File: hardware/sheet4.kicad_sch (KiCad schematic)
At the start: 16 parts, among them J2 B4B-XH-A, J3 B-2100S04P-A110, U2 STM32F072CBT6

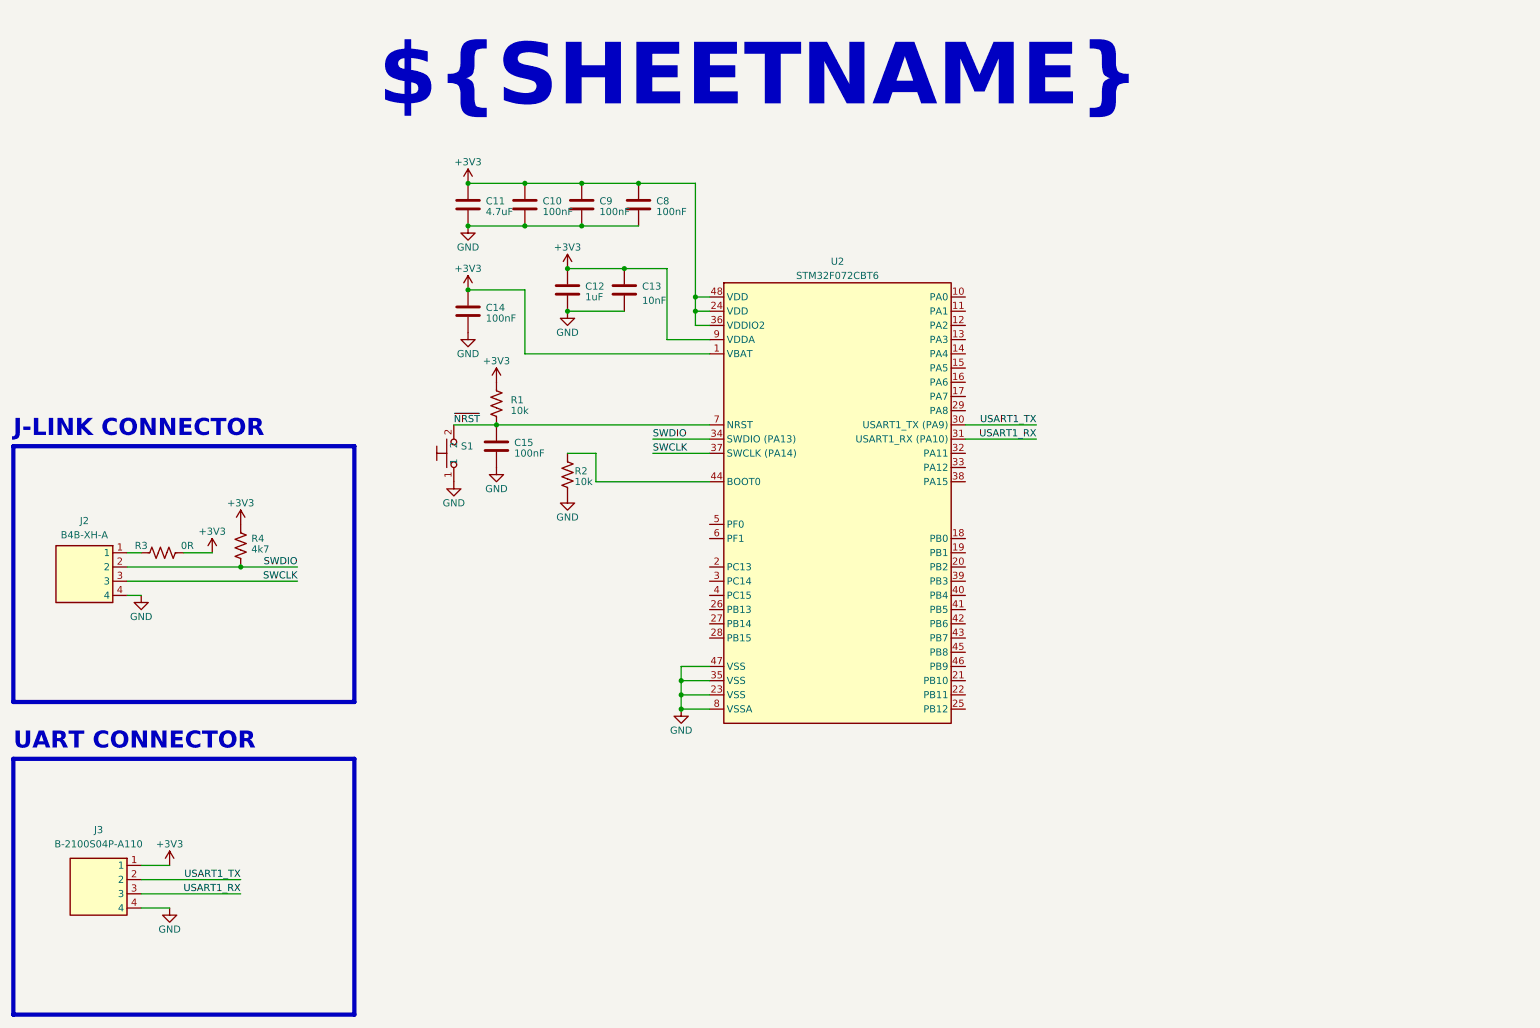
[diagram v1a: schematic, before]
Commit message: hardware(feat): add led indications
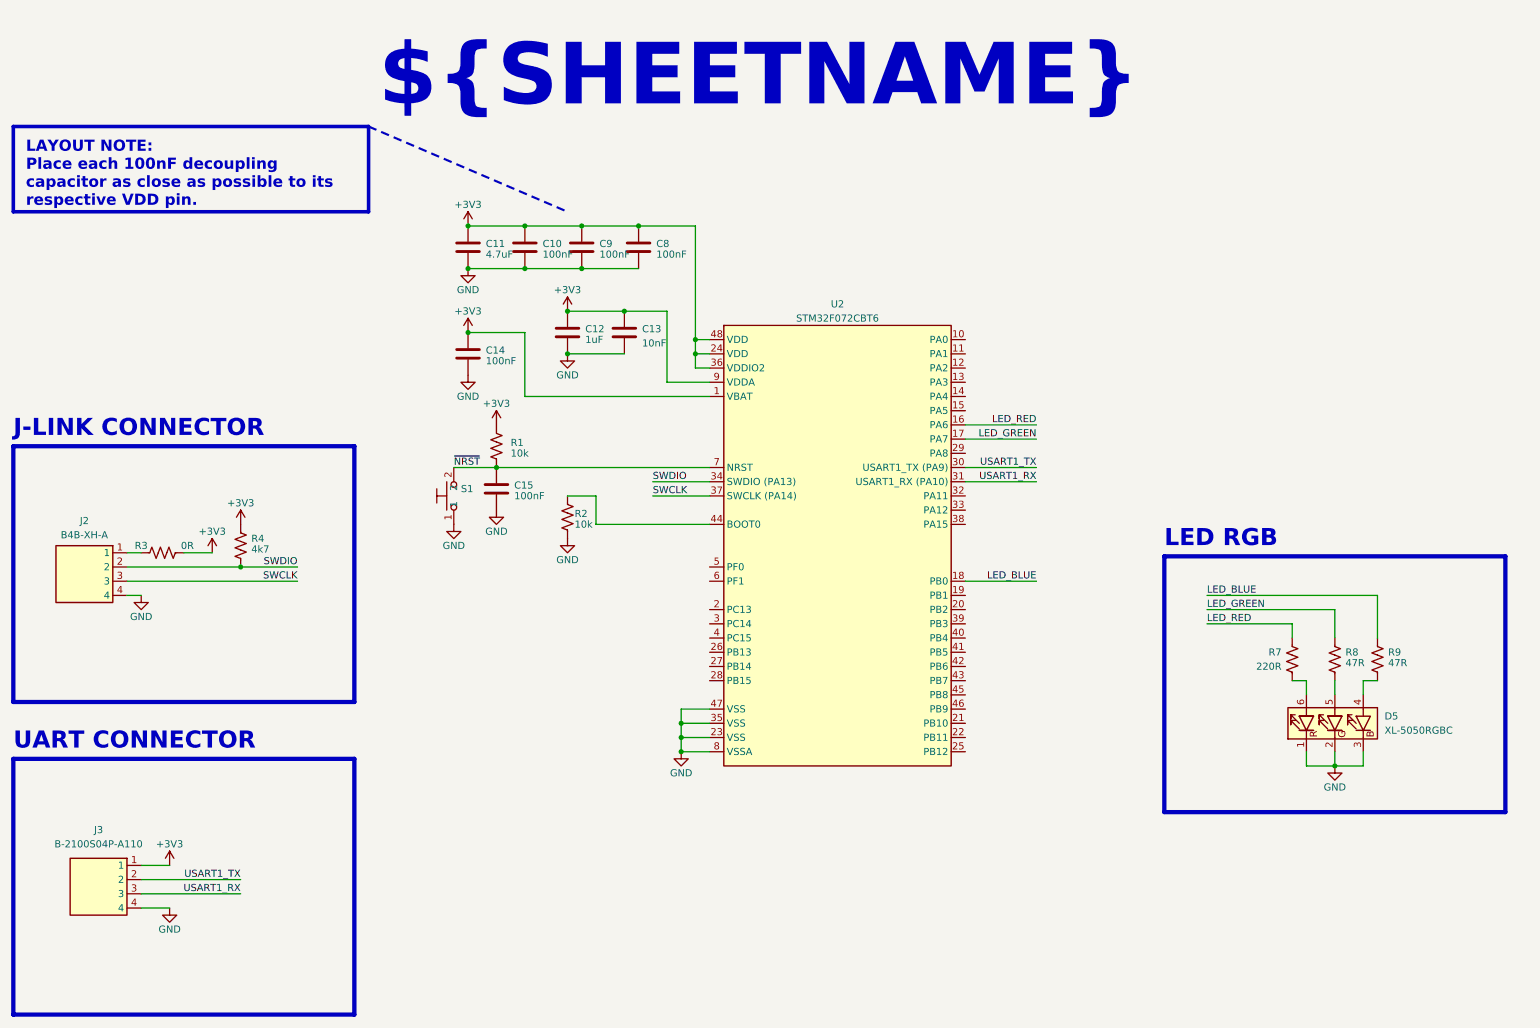
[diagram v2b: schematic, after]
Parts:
- added D5: XL-5050RGBC, 04_diodes:PLCC-6_XL-5050RGBC, symbol 04_diodes:LED_RGB-3.4V-20mA-PLCC-6
- added R7: 220R, 01_resistors:R_0603_1608Metric, symbol 01_resistors:RES_220R-0.1W-1%-0603
- added R8, R9: 47R, 01_resistors:R_0603_1608Metric, symbol 01_resistors:RES_47R-0.1W-1%-0603
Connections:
- net GND: now also D5.1 (RK), D5.2 (GK), D5.3 (BK)
- net LED_RED: now reaches U2.16 (PA6)
- net LED_RED: now also R7.1
- net LED_GREEN: now reaches U2.17 (PA7)
- net LED_GREEN: now also R8.1
- net LED_BLUE: now reaches U2.18 (PB0)
- net LED_BLUE: now also R9.1
- new net: D5.5 (GA), R8.2
- new net: D5.4 (BA), R9.2
- new net: D5.6 (RA), R7.2
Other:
- note added: "LED RGB"
- moved on the sheet: C10, C11, C12, C13, C14, C15, C8, C9, R1, R2, S1, U2

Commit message: hardware(feat): add usb connector with esd (#1)
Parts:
- added C20: 100nF, 02_capacitors:C_0603_1608Metric, symbol 02_capacitors:CAP_100nF-50V-10%-X7R-0603
- added D6: B5819W-TP, 04_diodes:D_SOD-123, symbol 04_diodes:DIO-S_40V-1A-0.6V-SOD-123
- added J4: U254-051N-4BH806, 08_connectors:SMD_U254-051N-4BH806, symbol 08_connectors:CON-USB_U254-051N-4BH806
- added U4: USBLC6-2SC6, 06_ics:SOT-23-6, symbol 06_ics:IC-IF_USBLC6-2SC6
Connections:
- net GND: now also C20.2, J4.5 (GND), J4.6 (SHIELD), U4.2 (GND)
- net USB_D_N: now reaches U2.32 (PA11)
- net USB_D_N: now also U4.3 (I/O2)
- net USB_D_P: now reaches U2.33 (PA12)
- net USB_D_P: now also U4.1 (I/O1)
- new net: J4.2 (D-), U4.4 (I/O2)
- new net: J4.3 (D+), U4.6 (I/O1)
- new net +5V: D6.1 (K)
- new net +VBUS: C20.1, D6.2 (A), J4.1 (VBUS), U4.5 (VBUS)
- no-connect marks 0 -> 1
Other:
- note added: "USB"

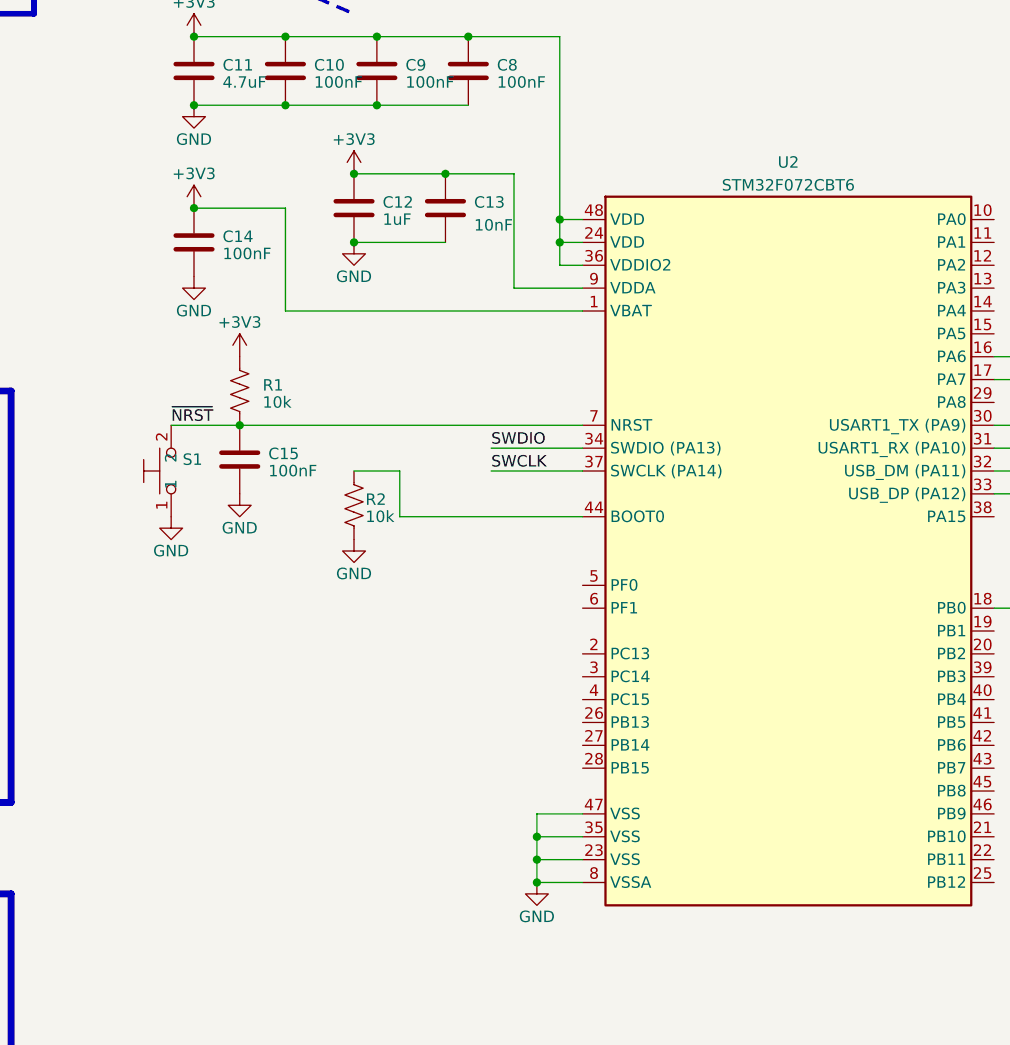
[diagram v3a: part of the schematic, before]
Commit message: hardware(feat): add rtc battery and lse crystal (#2)
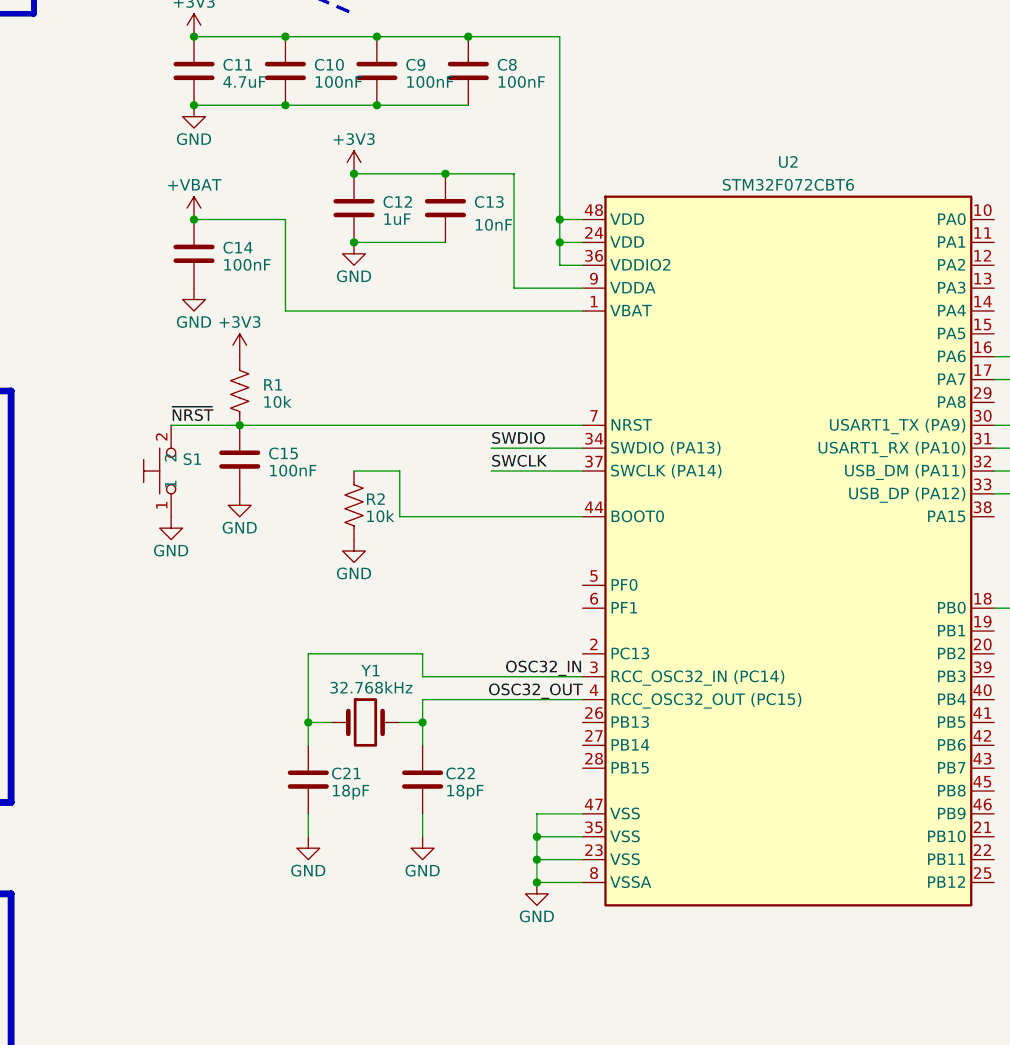
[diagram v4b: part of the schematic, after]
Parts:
- added C21, C22: 18pF, 02_capacitors:C_0603_1608Metric, symbol 02_capacitors:CAP_18pF-50V-5%-C0G-0603
- added Y1: 32.768kHz, 07_crystals:Crystal_SMD_3215-2Pin_3.2x1.5mm, symbol 07_crystals:XTAL_32.768kHz-Q13FC1350000400
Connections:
- net +3V3: no longer C14.1, U2.1 (VBAT)
- net GND: now also C21.2, C22.2
- net OSC32_IN: now reaches U2.3 (PC14)
- net OSC32_IN: now also C21.1, Y1.1
- net OSC32_OUT: now reaches U2.4 (PC15)
- net OSC32_OUT: now also C22.1, Y1.2
- new net +VBAT: C14.1, U2.1 (VBAT)
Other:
- moved on the sheet: C14

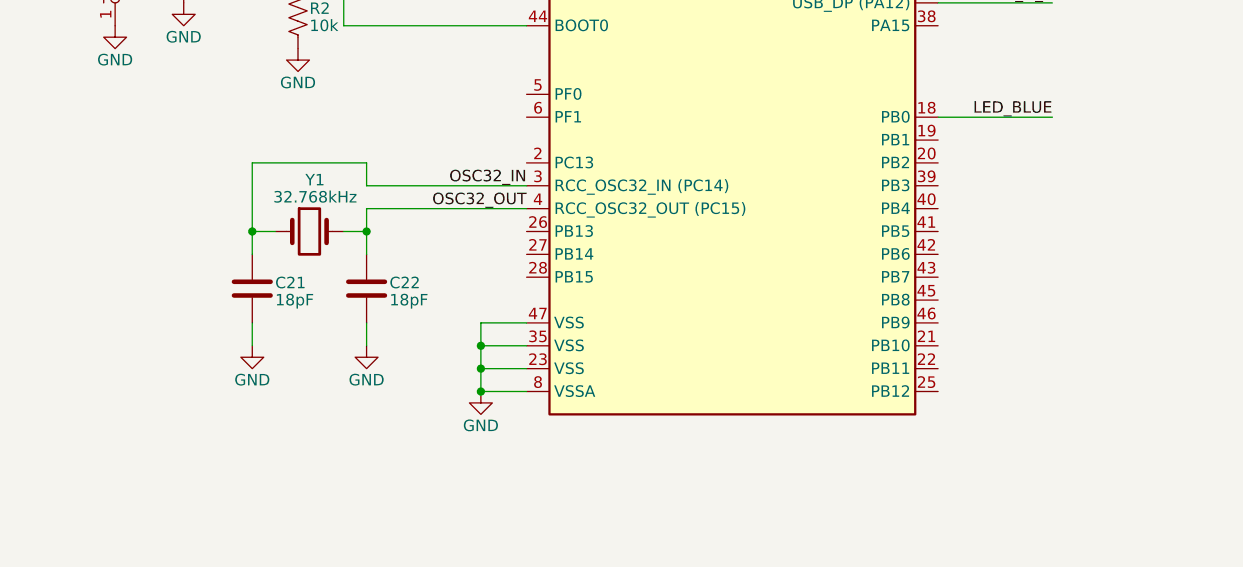
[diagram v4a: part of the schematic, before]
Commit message: hardware(feat): add spi nor flash with cs pull-up and decoupling (#6)
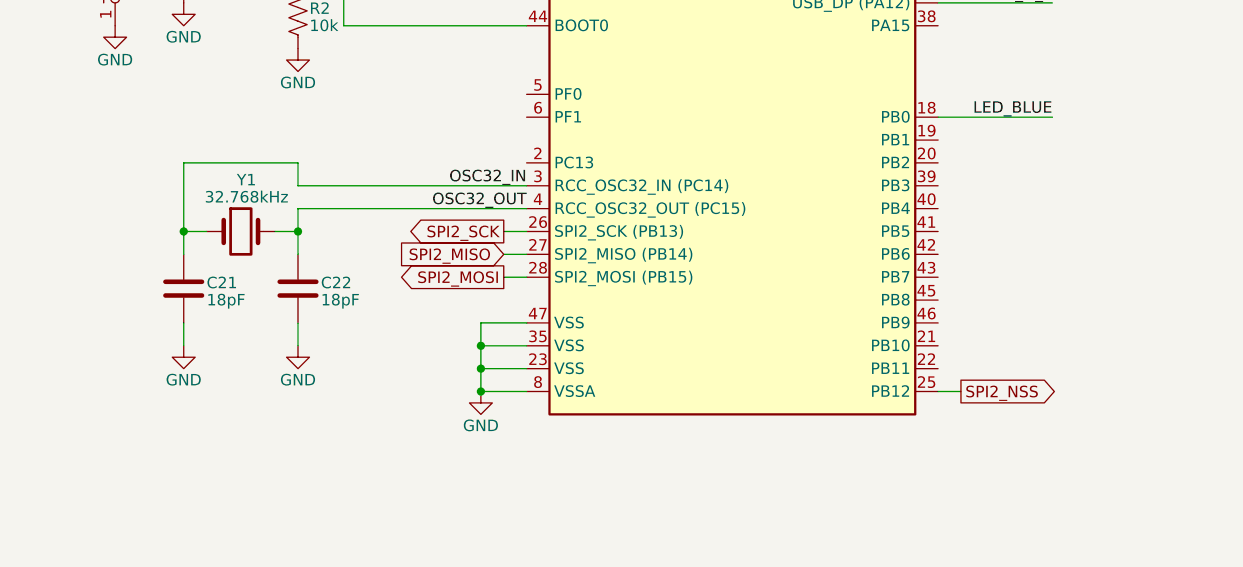
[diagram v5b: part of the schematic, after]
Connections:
- net SPI2_NSS: now reaches U2.25 (PB12)
- net SPI2_SCK: now reaches U2.26 (PB13)
- net SPI2_MISO: now reaches U2.27 (PB14)
- net SPI2_MOSI: now reaches U2.28 (PB15)
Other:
- moved on the sheet: C21, C22, Y1

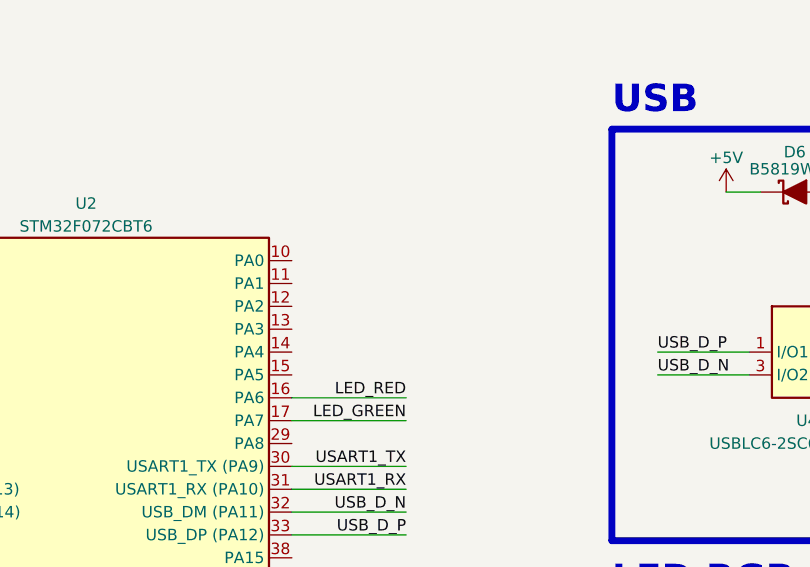
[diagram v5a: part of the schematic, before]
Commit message: hardware(feat): add push buttons with pull-ups and debounce (#3)
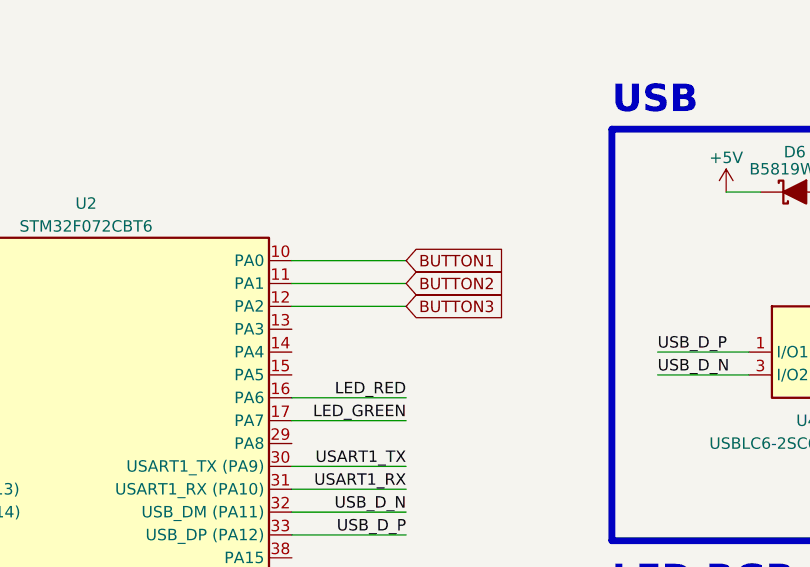
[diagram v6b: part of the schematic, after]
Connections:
- net BUTTON1: now reaches U2.10 (PA0)
- net BUTTON2: now reaches U2.11 (PA1)
- net BUTTON3: now reaches U2.12 (PA2)
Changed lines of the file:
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@@
+	(wire
+		(pts
+			(xy 185.42 73.66) (xy 198.12 73.66)
+		)
+		(stroke
+			(width 0)
+			(type default)
+		)
+	)
 	(wire
 		(pts
@@
 	(wire
 		(pts
+			(xy 185.42 78.74) (xy 198.12 78.74)
+		)
+		(stroke
+			(width 0)
+			(type default)
+		)
+	)
+	(wire
+		(pts
 			(xy 137.16 76.2) (xy 139.7 76.2)
 		)
@@
 		(pts
 			(xy 243.84 127) (xy 243.84 124.46)
+		)
+		(stroke
+			(width 0)
+			(type default)
+		)
+	)
+	(wire
+		(pts
+			(xy 185.42 76.2) (xy 198.12 76.2)
 		)
 		(stroke
@@
 				(hide yes)
 			)
+		)
+	)
+	(global_label "BUTTON3"
+		(shape input)
+		(at 198.12 78.74 0)
+		(fields_autoplaced yes)
+		(effects
+			(font
+				(size 1.27 1.27)
+			)
+			(justify left)
+		)
+		(property "Intersheetrefs" "${INTERSHEET_REFS}"
+			(at 209.5114 78.74 0)
+			(effects
+				(font
+					(size 1.27 1.27)
+				)
+				(justify left)
+				(hide yes)
+			)
+		)
+	)
+	(global_label "BUTTON1"
+		(shape input)
+		(at 198.12 73.66 0)
+		(fields_autoplaced yes)
+		(effects
+			(font
+				(size 1.27 1.27)
+			)
+			(justify left)
+		)
+		(property "Intersheetrefs" "${INTERSHEET_REFS}"
+			(at 209.5114 73.66 0)
+			(effects
+				(font
+					(size 1.27 1.27)
+				)
+				(justify left)
+				(hide yes)
+			)
+		)
+	)
+	(global_label "BUTTON2"
+		(shape input)
+		(at 198.12 76.2 0)
+		(fields_autoplaced yes)
+		(effects
+			(font
+				(size 1.27 1.27)
+			)
+			(justify left)
+		)
+		(property "Intersheetrefs" "${INTERSHEET_REFS}"
+			(at 209.5114 76.2 0)
+			(effects
+				(font
+					(size 1.27 1.27)
+				)
+				(justify left)
+				(hide yes)
+			)
